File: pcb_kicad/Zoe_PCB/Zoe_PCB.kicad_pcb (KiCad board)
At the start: 2 copper layers, 0 parts

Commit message: Saving PCB Diagram :D
Please don't erase it this time
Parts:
- added REF**: Zoe_DS1722, Zoe_PCB:Zoe_DS1722, F.Cu at (134.6, 95.9)
- added REF**: PinHeader_1x08_P2.54mm_Vertical, Connector_PinHeader_2.54mm:PinHeader_1x08_P2.54mm_Vertical, F.Cu at (124.5, 85.1)
- added REF**: PinHeader_1x08_P2.54mm_Vertical, Connector_PinHeader_2.54mm:PinHeader_1x08_P2.54mm_Vertical, F.Cu at (147.3, 85.1)
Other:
- board outline added: 27.9 x 28.6 mm
- board text added: "AN RST CS SCK MISO MOSI +3.3V GND"
- board text added: "PWM INT RX TX SCL SDA +5V GND"
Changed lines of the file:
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@@
   )
   (net 0 "")
+  (footprint "Zoe_PCB:Zoe_DS1722" (layer "F.Cu")
+    (at 134.62 95.885)
+    (attr smd)
+    (fp_text reference "REF**" (at 2.54 -7.62 unlocked) (layer "F.SilkS")
+        (effects (font (size 1 1) (thickness 0.1)))
+    )
+    (fp_text value "Zoe_DS1722" (at 5.08 10.16 unlocked) (layer "F.Fab")
+        (effects (font (size 1 1) (thickness 0.15)))
+    )
+    (fp_text user "${REFERENCE}" (at 2.54 12.7 unlocked) (layer "F.Fab")
+        (effects (font (size 1 1) (thickness 0.15)))
+    )
+    (fp_line (start -0.36 -5.97) (end 4.29 -5.97)
+      (stroke (width 0.1) (type default)) (layer "F.SilkS"))
+    (fp_line (start -0.36 0.89) (end -0.36 -5.97)
+      (stroke (width 0.1) (type default)) (layer "F.SilkS"))
+    (fp_line (start 4.29 0.89) (end -0.36 0.89)
+      (stroke (width 0.1) (type default)) (layer "F.SilkS"))
+    (fp_line (start 4.29 0.89) (end 4.29 -5.97)
+      (stroke (width 0.1) (type default)) (layer "F.SilkS"))
+    (fp_arc (start -0.360002 -3.048) (mid 0.148 -2.54) (end -0.360002 -2.032)
+      (stroke (width 0.1) (type default)) (layer "F.SilkS"))
+    (pad "1" smd roundrect (at 0 0) (size 0.72 1.78) (layers "F.Cu" "F.Paste" "F.Mask") (roundrect_rratio 0.125)
+      (solder_mask_margin 0.102))
+    (pad "2" smd roundrect (at 1.27 0) (size 0.72 1.78) (layers "F.Cu" "F.Paste" "F.Mask") (roundrect_rratio 0.125)
+      (solder_mask_margin 0.102))
+    (pad "3" smd roundrect (at 2.54 0) (size 0.72 1.78) (layers "F.Cu" "F.Paste" "F.Mask") (roundrect_rratio 0.125)
+      (solder_mask_margin 0.102))
+    (pad "4" smd roundrect (at 3.81 0) (size 0.72 1.78) (layers "F.Cu" "F.Paste" "F.Mask") (roundrect_rratio 0.125)
+      (solder_mask_margin 0.102))
+    (pad "5" smd roundrect (at 3.81 -4.68) (size 0.72 1.78) (layers "F.Cu" "F.Paste" "F.Mask") (roundrect_rratio 0.125)
+      (solder_mask_margin 0.102))
+    (pad "6" smd roundrect (at 2.54 -4.68) (size 0.72 1.78) (layers "F.Cu" "F.Paste" "F.Mask") (roundrect_rratio 0.125)
+      (solder_mask_margin 0.102))
+    (pad "7" smd roundrect (at 1.27 -4.68) (size 0.72 1.78) (layers "F.Cu" "F.Paste" "F.Mask") (roundrect_rratio 0.125)
+      (solder_mask_margin 0.102))
+    (pad "8" smd roundrect (at 0 -4.68) (size 0.72 1.78) (layers "F.Cu" "F.Paste" "F.Mask") (roundrect_rratio 0.125)
+      (solder_mask_margin 0.102))
+    (zone (net 0) (net_name "") (layer "F.SilkS") (name "SMD_chip") (hatch edge 0.5)
+      (connect_pads (clearance 0))
+      (min_thickness 0.25) (filled_areas_thickness no)
+      (keepout (tracks not_allowed) (vias not_allowed) (pads not_allowed) (copperpour allowed) (footprints allowed))
+      (fill (thermal_gap 0.5) (thermal_bridge_width 0.5))
+      (polygon
+        (pts
+          (xy 134.26 89.915)
+          (xy 138.91 89.915)
+          (xy 138.91 96.775)
+          (xy 134.26 96.775)
+        )
+      )
+    )
+  )
+  (footprint "Connector_PinHeader_2.54mm:PinHeader_1x08_P2.54mm_Vertical" (layer "F.Cu")
+    (at 124.46 85.09)
+    (descr "Through hole straight pin header, 1x08, 2.54mm pitch, single row")
+    (tags "Through hole pin header THT 1x08 2.54mm single row")
+    (attr through_hole)
+    (fp_text reference "REF**" (at 0 -2.33) (layer "F.SilkS")
+        (effects (font (size 1 1) (thickness 0.15)))
+    )
+    (fp_text value "PinHeader_1x08_P2.54mm_Vertical" (at -15.24 10.16) (layer "F.Fab")
+        (effects (font (size 1 1) (thickness 0.15)))
+    )
+    (fp_text user "${REFERENCE}" (at 0 8.89 90) (layer "F.Fab")
+        (effects (font (size 1 1) (thickness 0.15)))
+    )
+    (fp_line (start -1.33 -1.33) (end 0 -1.33)
+      (stroke (width 0.12) (type solid)) (layer "F.SilkS"))
+    (fp_line (start -1.33 0) (end -1.33 -1.33)
+      (stroke (width 0.12) (type solid)) (layer "F.SilkS"))
+    (fp_line (start -1.33 1.27) (end -1.33 19.11)
+      (stroke (width 0.12) (type solid)) (layer "F.SilkS"))
+    (fp_line (start -1.33 1.27) (end 1.33 1.27)
+      (stroke (width 0.12) (type solid)) (layer "F.SilkS"))
+    (fp_line (start -1.33 19.11) (end 1.33 19.11)
+      (stroke (width 0.12) (type solid)) (layer "F.SilkS"))
+    (fp_line (start 1.33 1.27) (end 1.33 19.11)
+      (stroke (width 0.12) (type solid)) (layer "F.SilkS"))
+    (fp_line (start -1.8 -1.8) (end -1.8 19.55)
+      (stroke (width 0.05) (type solid)) (layer "F.CrtYd"))
+    (fp_line (start -1.8 19.55) (end 1.8 19.55)
+      (stroke (width 0.05) (type solid)) (layer "F.CrtYd"))
+    (fp_line (start 1.8 -1.8) (end -1.8 -1.8)
+      (stroke (width 0.05) (type solid)) (layer "F.CrtYd"))
+    (fp_line (start 1.8 19.55) (end 1.8 -1.8)
+      (stroke (width 0.05) (type solid)) (layer "F.CrtYd"))
+    (fp_line (start -1.27 -0.635) (end -0.635 -1.27)
+      (stroke (width 0.1) (type solid)) (layer "F.Fab"))
+    (fp_line (start -1.27 19.05) (end -1.27 -0.635)
+      (stroke (width 0.1) (type solid)) (layer "F.Fab"))
+    (fp_line (start -0.635 -1.27) (end 1.27 -1.27)
+      (stroke (width 0.1) (type solid)) (layer "F.Fab"))
+    (fp_line (start 1.27 -1.27) (end 1.27 19.05)
+      (stroke (width 0.1) (type solid)) (layer "F.Fab"))
+    (fp_line (start 1.27 19.05) (end -1.27 19.05)
+      (stroke (width 0.1) (type solid)) (layer "F.Fab"))
+    (pad "1" thru_hole rect (at 0 0) (size 1.7 1.7) (drill 1) (layers "*.Cu" "*.Mask"))
+    (pad "2" thru_hole oval (at 0 2.54) (size 1.7 1.7) (drill 1) (layers "*.Cu" "*.Mask"))
+    (pad "3" thru_hole oval (at 0 5.08) (size 1.7 1.7) (drill 1) (layers "*.Cu" "*.Mask"))
+    (pad "4" thru_hole oval (at 0 7.62) (size 1.7 1.7) (drill 1) (layers "*.Cu" "*.Mask"))
+    (pad "5" thru_hole oval (at 0 10.16) (size 1.7 1.7) (drill 1) (layers "*.Cu" "*.Mask"))
+    (pad "6" thru_hole oval (at 0 12.7) (size 1.7 1.7) (drill 1) (layers "*.Cu" "*.Mask"))
+    (pad "7" thru_hole oval (at 0 15.24) (size 1.7 1.7) (drill 1) (layers "*.Cu" "*.Mask"))
+    (pad "8" thru_hole oval (at 0 17.78) (size 1.7 1.7) (drill 1) (layers "*.Cu" "*.Mask"))
+    (model "${KICAD6_3DMODEL_DIR}/Connector_PinHeader_2.54mm.3dshapes/PinHeader_1x08_P2.54mm_Vertical.wrl"
+      (offset (xyz 0 0 0))
+      (scale (xyz 1 1 1))
+      (rotate (xyz 0 0 0))
+    )
+  )
+  (footprint "Connector_PinHeader_2.54mm:PinHeader_1x08_P2.54mm_Vertical" (layer "F.Cu")
+    (at 147.32 85.09)
+    (descr "Through hole straight pin header, 1x08, 2.54mm pitch, single row")
+    (tags "Through hole pin header THT 1x08 2.54mm single row")
+    (attr through_hole)
+    (fp_text reference "REF**" (at 0 -2.33) (layer "F.SilkS")
+        (effects (font (size 1 1) (thickness 0.15)))
+    )
+    (fp_text value "PinHeader_1x08_P2.54mm_Vertical" (at 15.24 2.54) (layer "F.Fab")
+        (effects (font (size 1 1) (thickness 0.15)))
+    )
+    (fp_text user "${REFERENCE}" (at 0 8.89 90) (layer "F.Fab")
+        (effects (font (size 1 1) (thickness 0.15)))
+    )
+    (fp_line (start -1.33 -1.33) (end 0 -1.33)
+      (stroke (width 0.12) (type solid)) (layer "F.SilkS"))
+    (fp_line (start -1.33 0) (end -1.33 -1.33)
+      (stroke (width 0.12) (type solid)) (layer "F.SilkS"))
+    (fp_line (start -1.33 1.27) (end -1.33 19.11)
+      (stroke (width 0.12) (type solid)) (layer "F.SilkS"))
+    (fp_line (start -1.33 1.27) (end 1.33 1.27)
+      (stroke (width 0.12) (type solid)) (layer "F.SilkS"))
+    (fp_line (start -1.33 19.11) (end 1.33 19.11)
+      (stroke (width 0.12) (type solid)) (layer "F.SilkS"))
+    (fp_line (start 1.33 1.27) (end 1.33 19.11)
+      (stroke (width 0.12) (type solid)) (layer "F.SilkS"))
+    (fp_line (start -1.8 -1.8) (end -1.8 19.55)
+      (stroke (width 0.05) (type solid)) (layer "F.CrtYd"))
+    (fp_line (start -1.8 19.55) (end 1.8 19.55)
+      (stroke (width 0.05) (type solid)) (layer "F.CrtYd"))
+    (fp_line (start 1.8 -1.8) (end -1.8 -1.8)
+      (stroke (width 0.05) (type solid)) (layer "F.CrtYd"))
+    (fp_line (start 1.8 19.55) (end 1.8 -1.8)
+      (stroke (width 0.05) (type solid)) (layer "F.CrtYd"))
+    (fp_line (start -1.27 -0.635) (end -0.635 -1.27)
+      (stroke (width 0.1) (type solid)) (layer "F.Fab"))
+    (fp_line (start -1.27 19.05) (end -1.27 -0.635)
+      (stroke (width 0.1) (type solid)) (layer "F.Fab"))
+    (fp_line (start -0.635 -1.27) (end 1.27 -1.27)
+      (stroke (width 0.1) (type solid)) (layer "F.Fab"))
+    (fp_line (start 1.27 -1.27) (end 1.27 19.05)
+      (stroke (width 0.1) (type solid)) (layer "F.Fab"))
+    (fp_line (start 1.27 19.05) (end -1.27 19.05)
+      (stroke (width 0.1) (type solid)) (layer "F.Fab"))
+    (pad "1" thru_hole rect (at 0 0) (size 1.7 1.7) (drill 1) (layers "*.Cu" "*.Mask"))
+    (pad "2" thru_hole oval (at 0 2.54) (size 1.7 1.7) (drill 1) (layers "*.Cu" "*.Mask"))
+    (pad "3" thru_hole oval (at 0 5.08) (size 1.7 1.7) (drill 1) (layers "*.Cu" "*.Mask"))
+    (pad "4" thru_hole oval (at 0 7.62) (size 1.7 1.7) (drill 1) (layers "*.Cu" "*.Mask"))
+    (pad "5" thru_hole oval (at 0 10.16) (size 1.7 1.7) (drill 1) (layers "*.Cu" "*.Mask"))
+    (pad "6" thru_hole oval (at 0 12.7) (size 1.7 1.7) (drill 1) (layers "*.Cu" "*.Mask"))
+    (pad "7" thru_hole oval (at 0 15.24) (size 1.7 1.7) (drill 1) (layers "*.Cu" "*.Mask"))
+    (pad "8" thru_hole oval (at 0 17.78) (size 1.7 1.7) (drill 1) (layers "*.Cu" "*.Mask"))
+    (model "${KICAD6_3DMODEL_DIR}/Connector_PinHeader_2.54mm.3dshapes/PinHeader_1x08_P2.54mm_Vertical.wrl"
+      (offset (xyz 0 0 0))
+      (scale (xyz 1 1 1))
+      (rotate (xyz 0 0 0))
+    )
+  )
+  (gr_rect (start 121.92 80.645) (end 149.86 109.22)
+    (stroke (width 0.2) (type default)) (fill none) (layer "Edge.Cuts"))
+  (gr_text "PWM\nINT\nRX\nTX\nSCL\nSDA\n+5V\nGND" (at 144.78 103.505) (layer "F.SilkS")
+    (effects (font (size 1.5 1.5) (thickness 0.1016)) (justify right bottom))
+  )
+  (gr_text "AN\nRST\nCS\nSCK\nMISO\nMOSI\n+3.3V\nGND" (at 127 103.505) (layer "F.SilkS")
+    (effects (font (size 1.5 1.5) (thickness 0.1016)) (justify left bottom))
+  )
 )

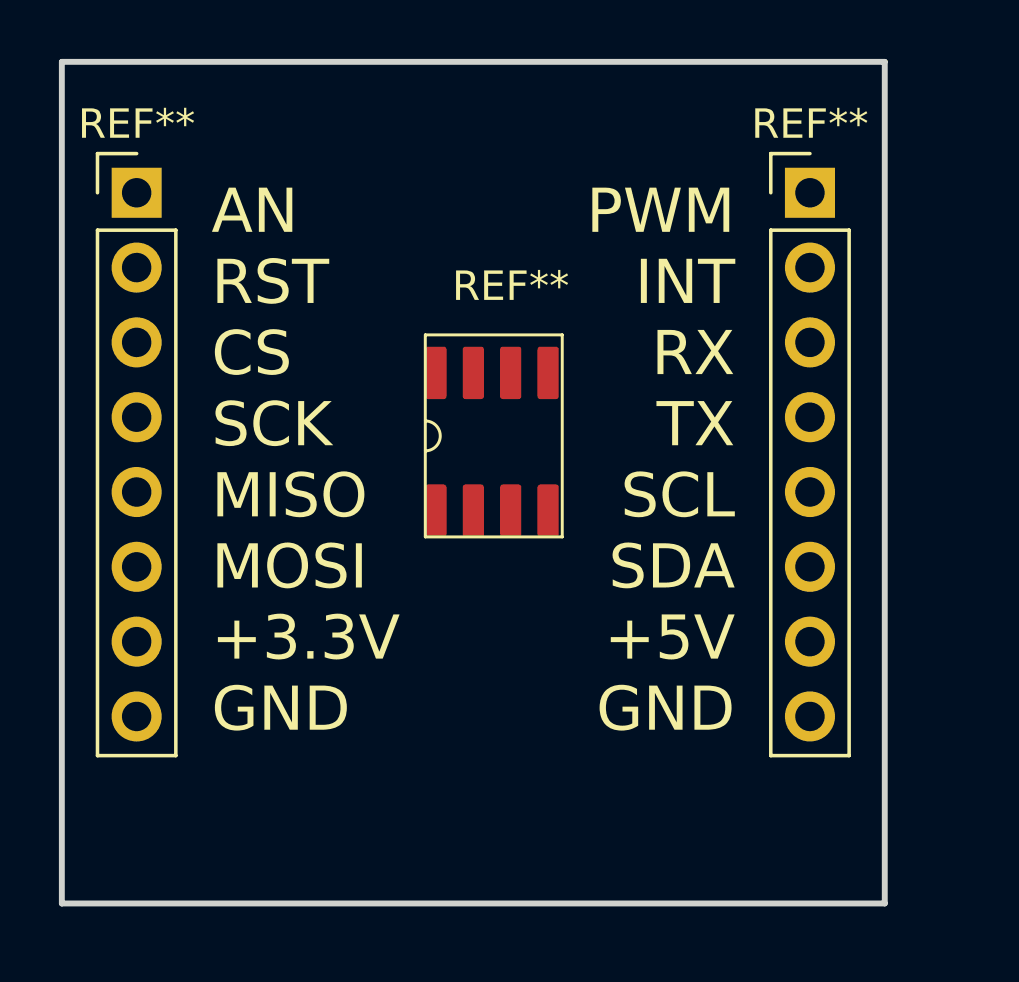
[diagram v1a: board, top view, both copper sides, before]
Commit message: Finished PCB board and confirmed readouts of motor
Finished programming PCB chip, also started checking the frequency of the motor in lab, and it appears to be correct :) -- need to add additional algorithms for excellence.
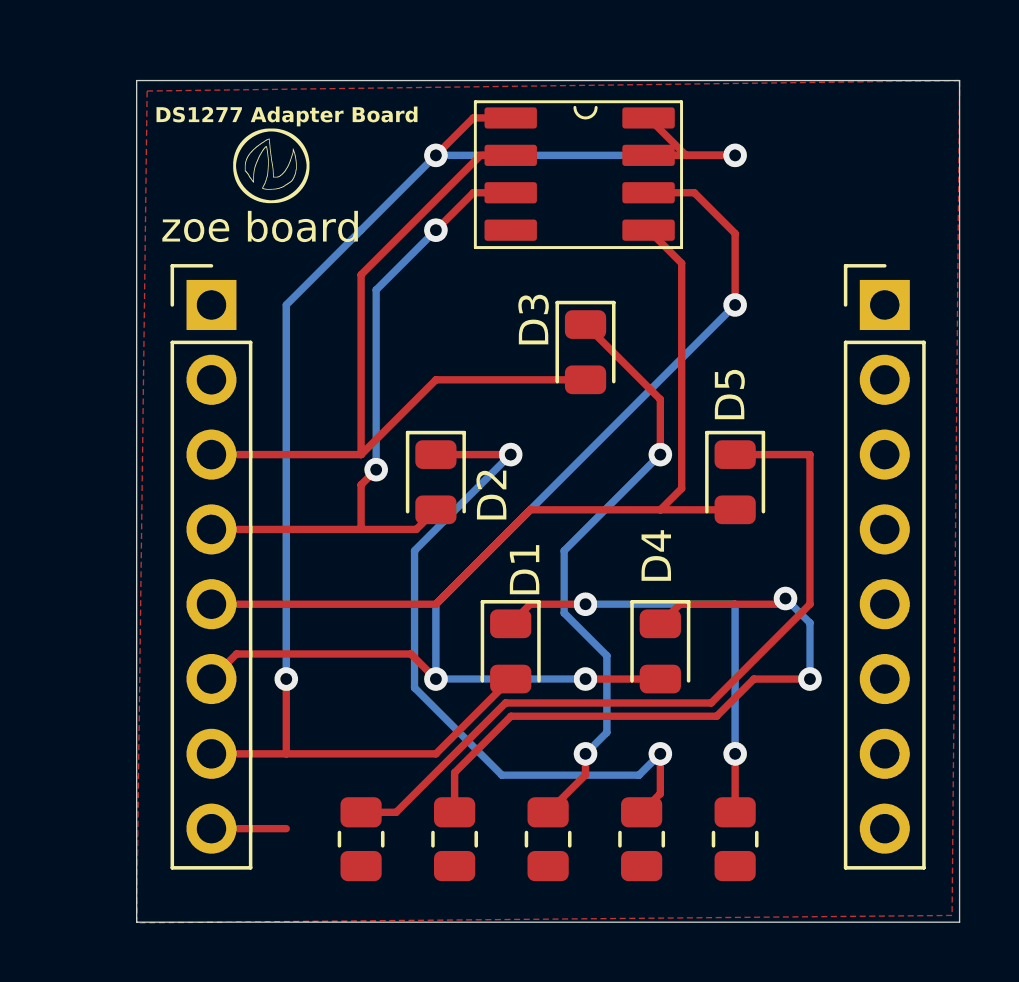
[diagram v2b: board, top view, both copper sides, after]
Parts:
- removed REF**: Zoe_DS1722, Zoe_PCB:Zoe_DS1722
- removed REF** (x2): PinHeader_1x08_P2.54mm_Vertical, Connector_PinHeader_2.54mm:PinHeader_1x08_P2.54mm_Vertical
- added D1: LED, LED_SMD:LED_0805_2012Metric, F.Cu at (137.2, 100.7)
- added D2: LED, LED_SMD:LED_0805_2012Metric, F.Cu at (134.6, 94.9)
- added D3: LED, LED_SMD:LED_0805_2012Metric, F.Cu at (139.7, 90.5)
- added D4: LED, LED_SMD:LED_0805_2012Metric, F.Cu at (142.2, 100.7)
- added D5: LED, LED_SMD:LED_0805_2012Metric, F.Cu at (144.8, 94.9)
- added G***: LOGO, Zoe_PCB:zoe_logo, F.Cu at (128.9, 84.2)
- added J1: Conn_01x08, Connector_PinHeader_2.54mm:PinHeader_1x08_P2.54mm_Vertical, F.Cu at (127.0, 88.9)
- added J2: Conn_01x08, Connector_PinHeader_2.54mm:PinHeader_1x08_P2.54mm_Vertical, F.Cu at (149.9, 88.9)
- added R1: 1k, Resistor_SMD:R_0805_2012Metric, F.Cu at (144.8, 107.0)
- added R2: 1k, Resistor_SMD:R_0805_2012Metric, F.Cu at (141.6, 107.0)
- added R3: 1k, Resistor_SMD:R_0805_2012Metric, F.Cu at (138.4, 107.0)
- added R4: 1k, Resistor_SMD:R_0805_2012Metric, F.Cu at (135.3, 107.0)
- added R5: 1k, Resistor_SMD:R_0805_2012Metric, F.Cu at (132.1, 107.0)
- added U1: ~, Zoe_PCB:Zoe_DS1722, F.Cu at (137.2, 82.5)
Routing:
- net /+3.3V: track 0.00 -> 53.3 mm, vias 0 -> 3
- net /MOSI: track 0.00 -> 38.8 mm, vias 0 -> 3
- net /MISO: track 0.00 -> 29.4 mm
- net /CS: track 0.00 -> 26.6 mm
- net Net-(D5-K): track 0.00 -> 25.8 mm
- net Net-(D2-K): track 0.00 -> 23.9 mm, vias 0 -> 2
- net Net-(D4-K): track 0.00 -> 22.4 mm, vias 0 -> 2
- net /SCK: track 0.00 -> 22.2 mm, vias 0 -> 2
- net Net-(D3-K): track 0.00 -> 20.4 mm, vias 0 -> 2
- net Net-(D1-K): track 0.00 -> 15.0 mm, vias 0 -> 2
- net GND: track 0.00 -> 2.54 mm
- added copper zone on F.Cu, net GND
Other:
- rule pad_to_mask_clearance: 0.0508 -> 0
- board text added: "DS1277 Adapter Board"
- board text added: "zoe board"
